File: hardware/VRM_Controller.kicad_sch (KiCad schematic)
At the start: 33 parts, among them J2001 Conn_01x02_Pin, J2002 Conn_01x02_Pin, J2003 Conn_01x02_Pin, J2004 Conn_01x02_Pin, U2001 TPS536C7B1RSLT

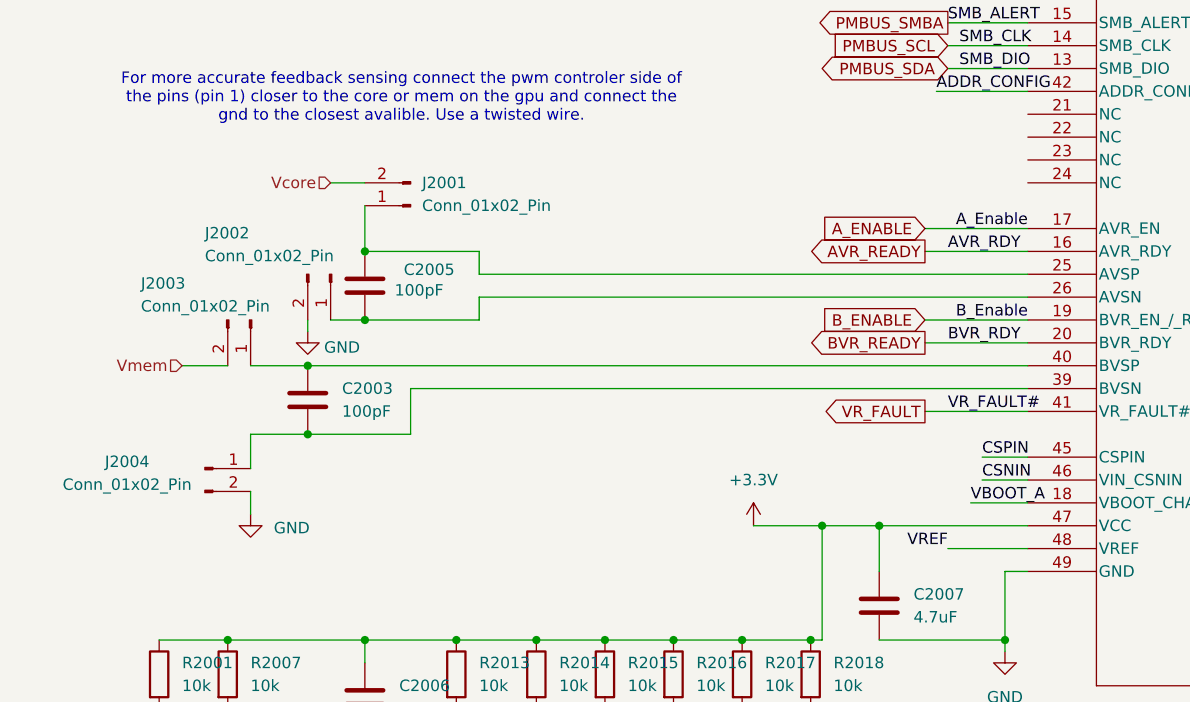
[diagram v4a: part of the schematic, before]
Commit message: feat(pcb): change feedback connectors to 2x2 instead of 2 1x2s
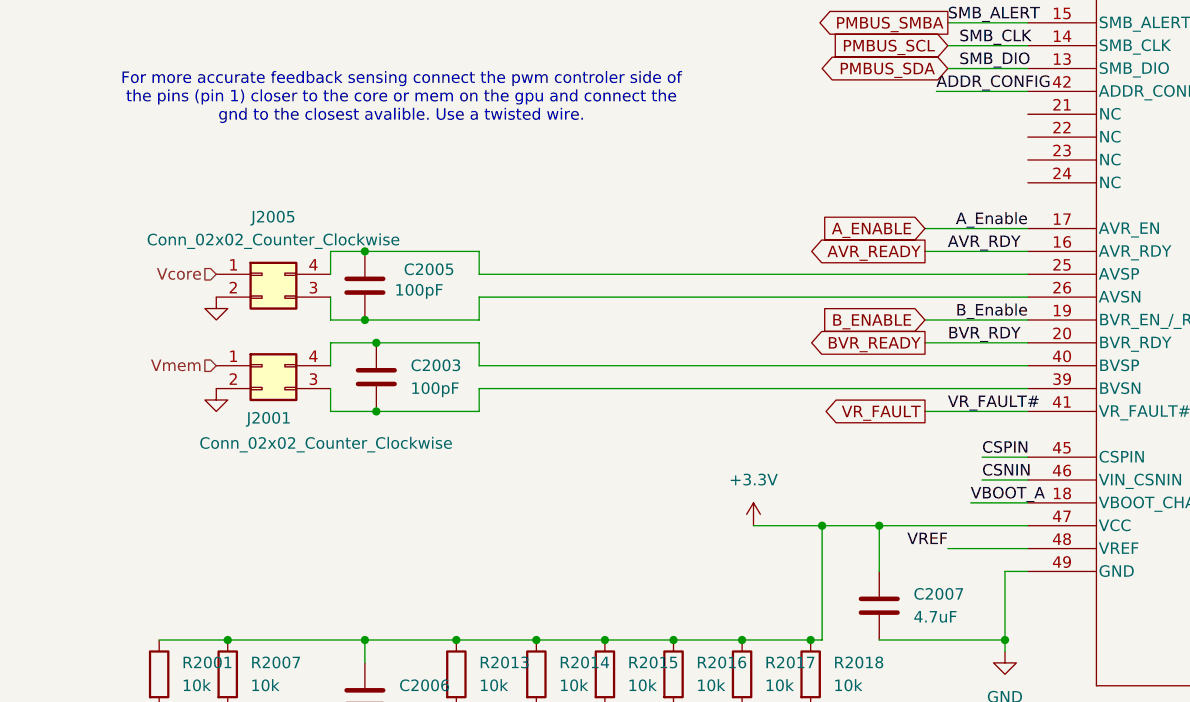
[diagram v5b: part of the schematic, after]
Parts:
- removed J2001, J2002, J2003, J2004: Conn_01x02_Pin, Connector_PinHeader_2.54mm:PinHeader_1x02_P2.54mm_Vertical_SMD_Pin1Left, symbol Connector:Conn_01x02_Pin
- added J2001, J2005: Conn_02x02_Counter_Clockwise, Connector_PinHeader_2.54mm:PinHeader_2x02_P2.54mm_Vertical, symbol Connector_Generic:Conn_02x02_Counter_Clockwise
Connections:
- net GND: now also J2001.2 (Pin_2), J2005.2 (Pin_2)
- net Vcore: now also J2005.1 (Pin_1)
- net Vmem: now also J2001.1 (Pin_1)
- net at C2005.1, U2001.25 (AVSP): now also J2005.4 (Pin_4)
- net at C2005.2, U2001.26 (AVSN): now also J2005.3 (Pin_3)
- net at C2003.1, U2001.40 (BVSP): now also J2001.4 (Pin_4)
- net at C2003.2, U2001.39 (BVSN): now also J2001.3 (Pin_3)
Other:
- moved on the sheet: C2003

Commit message: chore(schematic): add LCSC Part Numbers
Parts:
- C2001, C2004: LCSC Part Number (none) -> C1523
- C2002, C2010, C2011, C2012: LCSC Part Number (none) -> C14445
- C2003, C2005: LCSC Part Number (none) -> C1546
- C2006: LCSC Part Number (none) -> C1581
- C2007: LCSC Part Number (none) -> C23733
- C2008, C2009: LCSC Part Number (none) -> C1530
- J2001, J2005: LCSC Part Number (none) -> C66690
- R2001, R2002, R2007, R2008: LCSC Part Number (none) -> C17414
- R2003, R2010: LCSC Part Number (none) -> C22795
- R2004, R2011: LCSC Part Number (none) -> C25888
- R2013, R2014, R2015, R2016, R2017, R2018: LCSC Part Number (none) -> C100126
- R2019, R2020: LCSC Part Number (none) -> C252657
- U2001: LCSC Part Number (none) -> C3189587

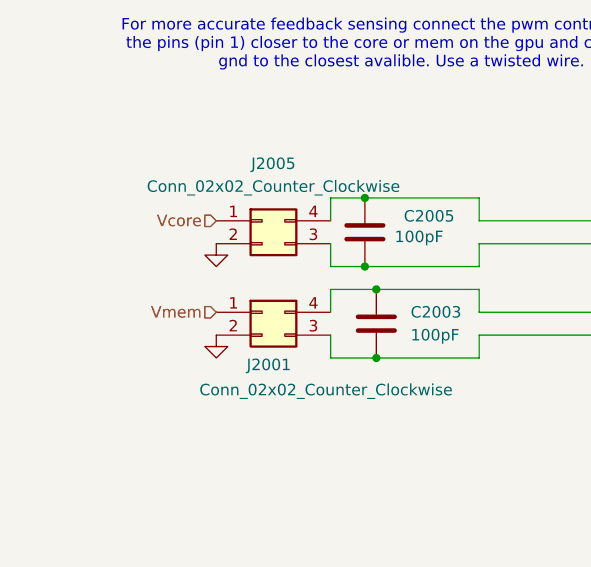
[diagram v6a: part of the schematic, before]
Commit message: fix(hardware): fixes for prototype 2
Fixes:
* SMBA text orientation wrong
* Proper pinout for Vmem and Vcore feedback
* Microcontroller
  * VSSA connection to gnd
  * VRef+ connection to 3.3V
  * VCap connection to 4.7uF to gnd
* Adjust Mask between Vmem and Vcore Planes
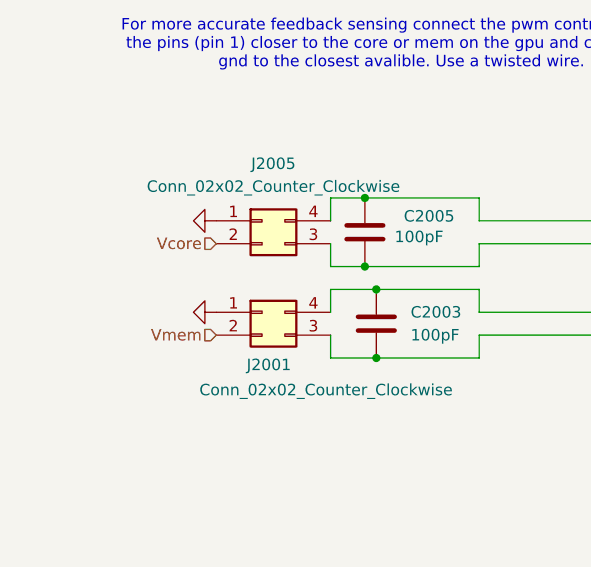
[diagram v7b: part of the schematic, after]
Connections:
- net GND: now also J2001.1 (Pin_1), J2005.1 (Pin_1); no longer J2001.2 (Pin_2), J2005.2 (Pin_2)
- net Vcore: now also J2005.2 (Pin_2); no longer J2005.1 (Pin_1)
- net Vmem: now also J2001.2 (Pin_2); no longer J2001.1 (Pin_1)
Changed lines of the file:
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@@
 	(hierarchical_label "Vmem"
 		(shape input)
-		(at 31.75 99.06 180)
+		(at 31.75 101.6 180)
 		(effects
 			(font
@@
 	(hierarchical_label "Vcore"
 		(shape input)
-		(at 31.75 88.9 180)
+		(at 31.75 91.44 180)
 		(effects
 			(font
@@
 	(symbol
 		(lib_id "power:GND")
-		(at 31.75 91.44 0)
+		(at 31.75 88.9 270)
 		(unit 1)
 		(exclude_from_sim no)
@@
 		(dnp no)
 		(property "Reference" "#PWR02004"
-			(at 31.75 97.79 0)
+			(at 25.4 88.9 0)
 			(effects
 				(font
@@
 		)
 		(property "Value" "GND"
-			(at 35.56 93.218 0)
+			(at 29.972 92.71 0)
 			(effects
 				(font
@@
 		)
 		(property "Footprint" ""
-			(at 31.75 91.44 0)
+			(at 31.75 88.9 0)
 			(effects
 				(font
@@
 		)
 		(property "Datasheet" ""
-			(at 31.75 91.44 0)
+			(at 31.75 88.9 0)
 			(effects
 				(font
@@
 		)
 		(property "Description" "Power symbol creates a global label with name \"GND\" , ground"
-			(at 31.75 91.44 0)
+			(at 31.75 88.9 0)
 			(effects
 				(font
@@
 	(symbol
 		(lib_id "power:GND")
-		(at 31.75 101.6 0)
+		(at 31.75 99.06 270)
 		(unit 1)
 		(exclude_from_sim no)
@@
 		(dnp no)
 		(property "Reference" "#PWR02002"
-			(at 31.75 107.95 0)
+			(at 25.4 99.06 0)
 			(effects
 				(font
@@
 		)
 		(property "Value" "GND"
-			(at 36.322 103.124 0)
+			(at 30.226 103.632 0)
 			(effects
 				(font
@@
 		)
 		(property "Footprint" ""
-			(at 31.75 101.6 0)
+			(at 31.75 99.06 0)
 			(effects
 				(font
@@
 		)
 		(property "Datasheet" ""
-			(at 31.75 101.6 0)
+			(at 31.75 99.06 0)
 			(effects
 				(font
@@
 		)
 		(property "Description" "Power symbol creates a global label with name \"GND\" , ground"
-			(at 31.75 101.6 0)
+			(at 31.75 99.06 0)
 			(effects
 				(font
